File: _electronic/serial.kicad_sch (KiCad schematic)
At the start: 11 parts

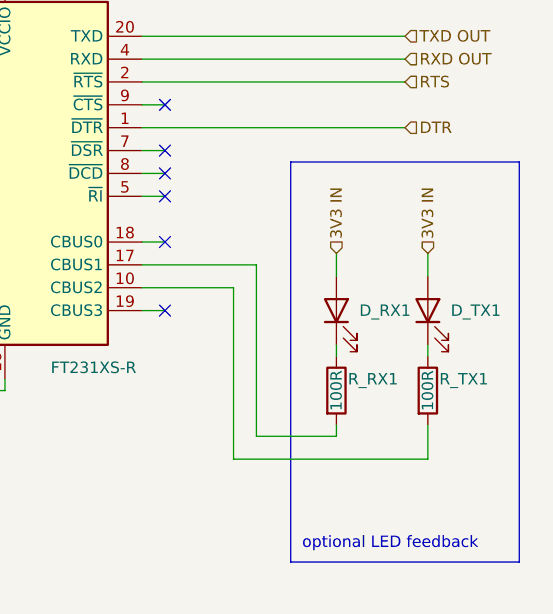
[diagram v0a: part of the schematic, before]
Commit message: BETA first upload
nothing major done here:
* updated KiCAD files to v9
* removed alternative 6v feed-in. The proposed buck converter is fine.
* added to all components LCSC component IDs. With this, exporting the project as gerber files also automatically creates correct BOM for JLCPCB manufacturing
*
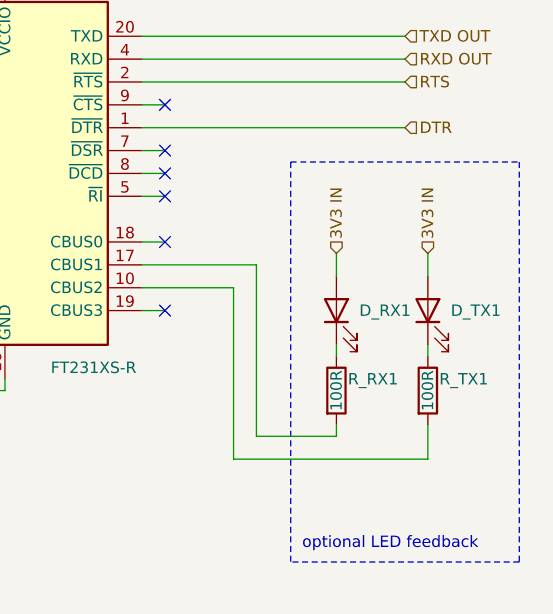
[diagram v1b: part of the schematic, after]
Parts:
- C_SER2, C_SER3: LCSC (none) -> C1671
- C_SER4: LCSC (none) -> C14663
- C_SER5: LCSC (none) -> C96446
- D_RX1, D_TX1: LCSC (none) -> C2290
- R_RX1, R_TX1: LCSC (none) -> C22775
- R_SER1, R_SER2: LCSC (none) -> C25190
- U_SER1: LCSC (none) -> C132160
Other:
- title: E-TKT v1.0 -> E-TKT v2.0 BETA

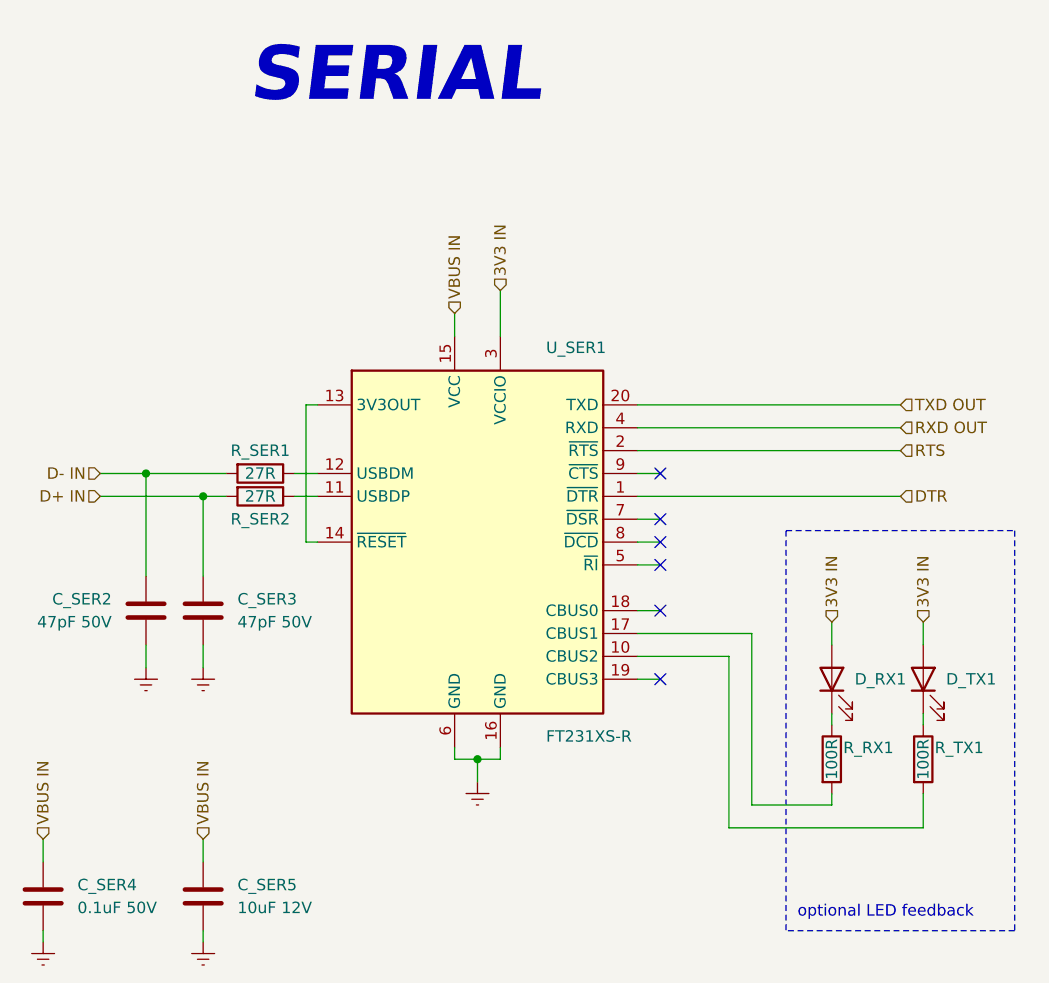
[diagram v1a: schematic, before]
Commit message: Updated layout of schematic symbol's text
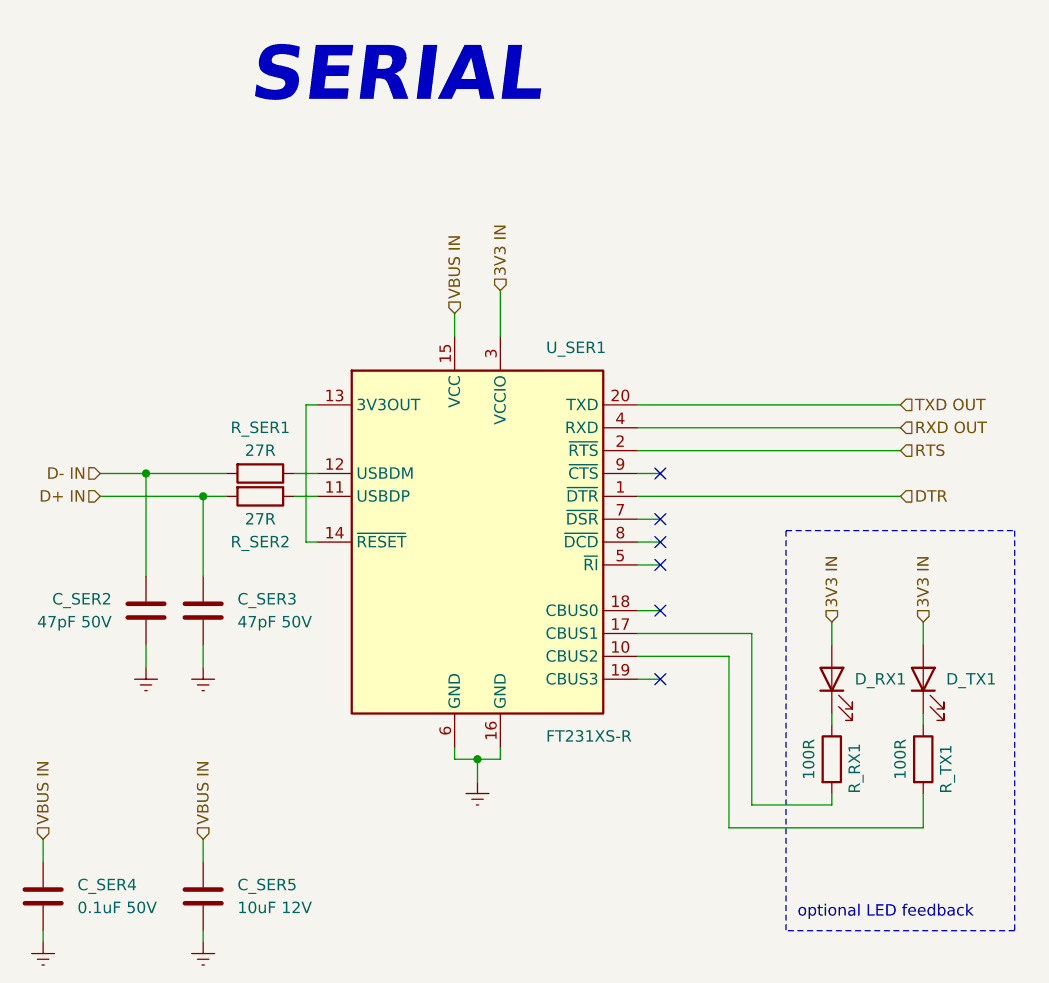
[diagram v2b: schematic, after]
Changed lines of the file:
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@@
 		(dnp no)
 		(property "Reference" "R_SER1"
+			(at 125.73 80.01 90)
+			(effects
+				(font
+					(size 1.27 1.27)
+				)
+			)
+		)
+		(property "Value" "27R"
 			(at 125.73 82.55 90)
-			(effects
-				(font
-					(size 1.27 1.27)
-				)
-			)
-		)
-		(property "Value" "27R"
-			(at 125.73 85.09 90)
 			(effects
 				(font
@@
 		(dnp no)
 		(property "Reference" "R_RX1"
-			(at 190.5 115.57 0)
+			(at 191.77 120.65 90)
 			(effects
 				(font
@@
 		)
 		(property "Value" "100R"
-			(at 189.23 116.84 90)
+			(at 186.69 116.84 90)
 			(effects
 				(font
@@
 		(dnp no)
 		(property "Reference" "R_SER2"
+			(at 125.73 92.71 90)
+			(effects
+				(font
+					(size 1.27 1.27)
+				)
+			)
+		)
+		(property "Value" "27R"
 			(at 125.73 90.17 90)
-			(effects
-				(font
-					(size 1.27 1.27)
-				)
-			)
-		)
-		(property "Value" "27R"
-			(at 125.73 87.63 90)
 			(effects
 				(font
@@
 		(dnp no)
 		(property "Reference" "R_TX1"
-			(at 200.66 115.57 0)
+			(at 201.93 120.65 90)
 			(effects
 				(font
@@
 		)
 		(property "Value" "100R"
-			(at 199.39 116.84 90)
-			(effects
-				(font
+			(at 196.85 116.84 90)
+			(effects
+				(font
